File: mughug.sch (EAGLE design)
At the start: 9 parts, among them J1 NEOPIXEL, U1 DS18B20

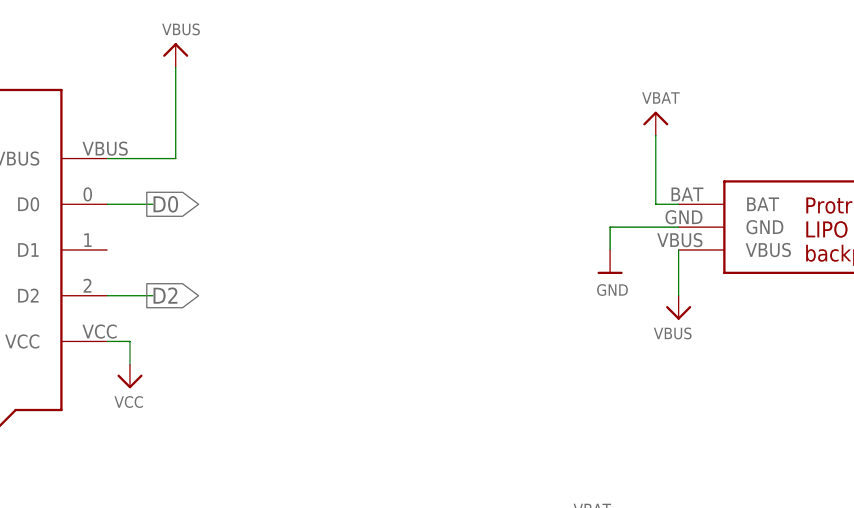
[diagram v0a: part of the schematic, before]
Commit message: Board reshuffle for oshpark
Added thicker board outline
moved neopixel to board center
small passived aligned same direction
12mil track for VBAT
added silkscreen
added corner holes for attachment
crossed fingers
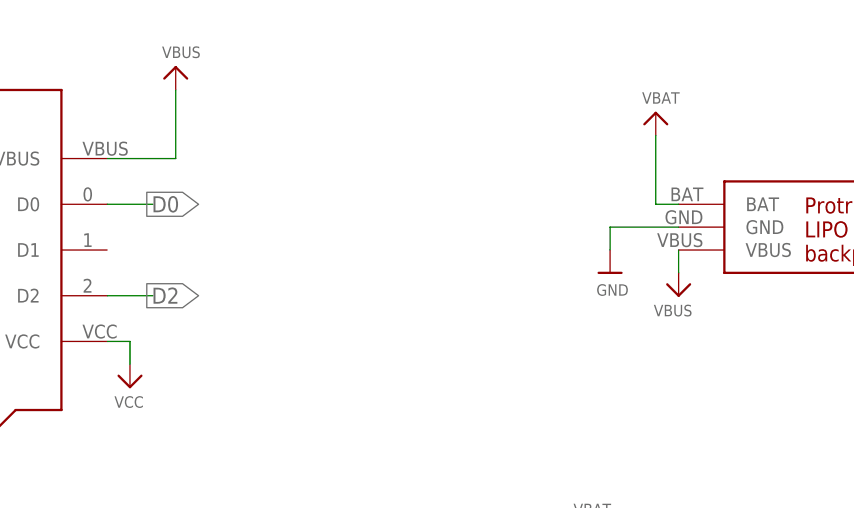
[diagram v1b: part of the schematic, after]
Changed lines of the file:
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@@
 <pinref part="U$3" gate="G$1" pin="VBUS"/>
 <wire x1="55.88" y1="88.9" x2="63.5" y2="88.9" width="0.1524" layer="91"/>
-<wire x1="63.5" y1="88.9" x2="63.5" y2="99.06" width="0.1524" layer="91"/>
+<wire x1="63.5" y1="88.9" x2="63.5" y2="96.52" width="0.1524" layer="91"/>
 </segment>
 <segment>
 <pinref part="U$2" gate="G$1" pin="VBUS"/>
 <pinref part="U$4" gate="G$1" pin="VBUS"/>
-<wire x1="119.38" y1="78.74" x2="119.38" y2="73.66" width="0.1524" layer="91"/>
+<wire x1="119.38" y1="78.74" x2="119.38" y2="76.2" width="0.1524" layer="91"/>
 </segment>
 </net>

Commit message: Final tweak for oshpark proto order
oshpark order dm4ze97u
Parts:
- U$2: value PROTRINKETLIPONOHOLE -> PROTRINKETLIPO; device redhunter:PROTRINKETLIPONOHOLE -> redhunter:PROTRINKETLIPO
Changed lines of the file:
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@@
 <parts>
 <part name="U$1" library="redhunter" deviceset="TRINKET" device="NOHOLES"/>
-<part name="U$2" library="redhunter" deviceset="PROTRINKETLIPO" device="NOHOLE"/>
+<part name="U$2" library="redhunter" deviceset="PROTRINKETLIPO" device="" value="PROTRINKETLIPO"/>
 <part name="VBAT" library="microbuilder" deviceset="VBAT" device=""/>
 <part name="U$3" library="microbuilder" deviceset="VBUS" device=""/>
